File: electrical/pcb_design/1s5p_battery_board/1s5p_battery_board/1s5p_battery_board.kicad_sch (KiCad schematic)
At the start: 0 parts

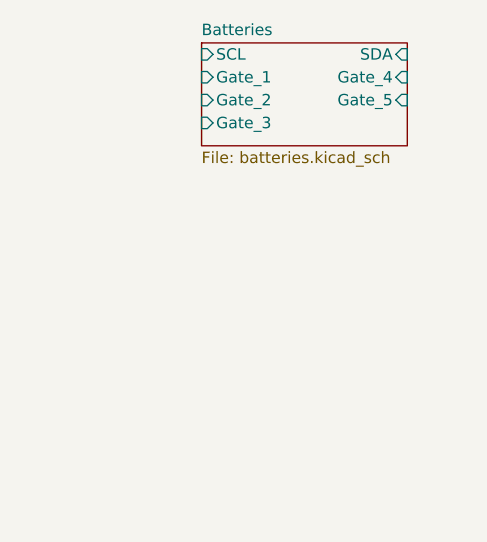
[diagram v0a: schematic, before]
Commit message: mosfet on battery board flipped
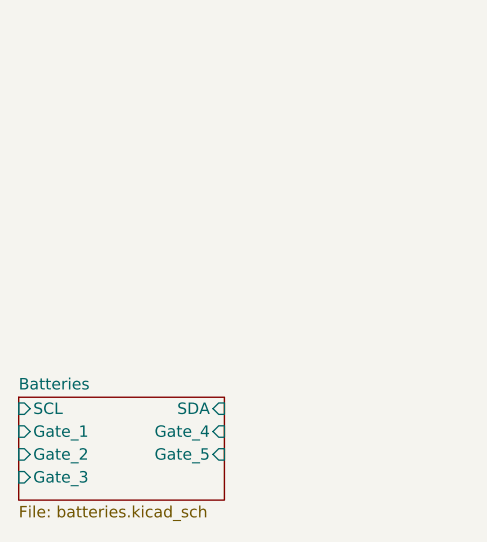
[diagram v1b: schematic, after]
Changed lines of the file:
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@@
 	(paper "A4")
 	(sheet
-		(at 60.96 116.84)
+		(at 40.64 156.21)
 		(size 22.86 11.43)
 		(fields_autoplaced yes)
@@
 		)
 		(property "Sheetname" "Batteries"
-			(at 60.96 116.1284 0)
+			(at 40.64 155.4984 0)
 			(effects
 				(font
@@
 		)
 		(property "Sheetfile" "batteries.kicad_sch"
-			(at 60.96 128.8546 0)
+			(at 40.64 168.2246 0)
 			(effects
 				(font
@@
 		)
 		(pin "Gate_5" input
-			(at 83.82 123.19 0)
+			(at 63.5 162.56 0)
 			(effects
 				(font
@@
 		)
 		(pin "Gate_2" input
-			(at 60.96 123.19 180)
+			(at 40.64 162.56 180)
 			(effects
 				(font
@@
 		)
 		(pin "SCL" input
-			(at 60.96 118.11 180)
+			(at 40.64 157.48 180)
 			(effects
 				(font
@@
 		)
 		(pin "SDA" input
-			(at 83.82 118.11 0)
+			(at 63.5 157.48 0)
 			(effects
 				(font
@@
 		)
 		(pin "Gate_3" input
-			(at 60.96 125.73 180)
+			(at 40.64 165.1 180)
 			(effects
 				(font
@@
 		)
 		(pin "Gate_1" input
-			(at 60.96 120.65 180)
+			(at 40.64 160.02 180)
 			(effects
 				(font
@@
 		)
 		(pin "Gate_4" input
-			(at 83.82 120.65 0)
+			(at 63.5 160.02 0)
 			(effects
 				(font

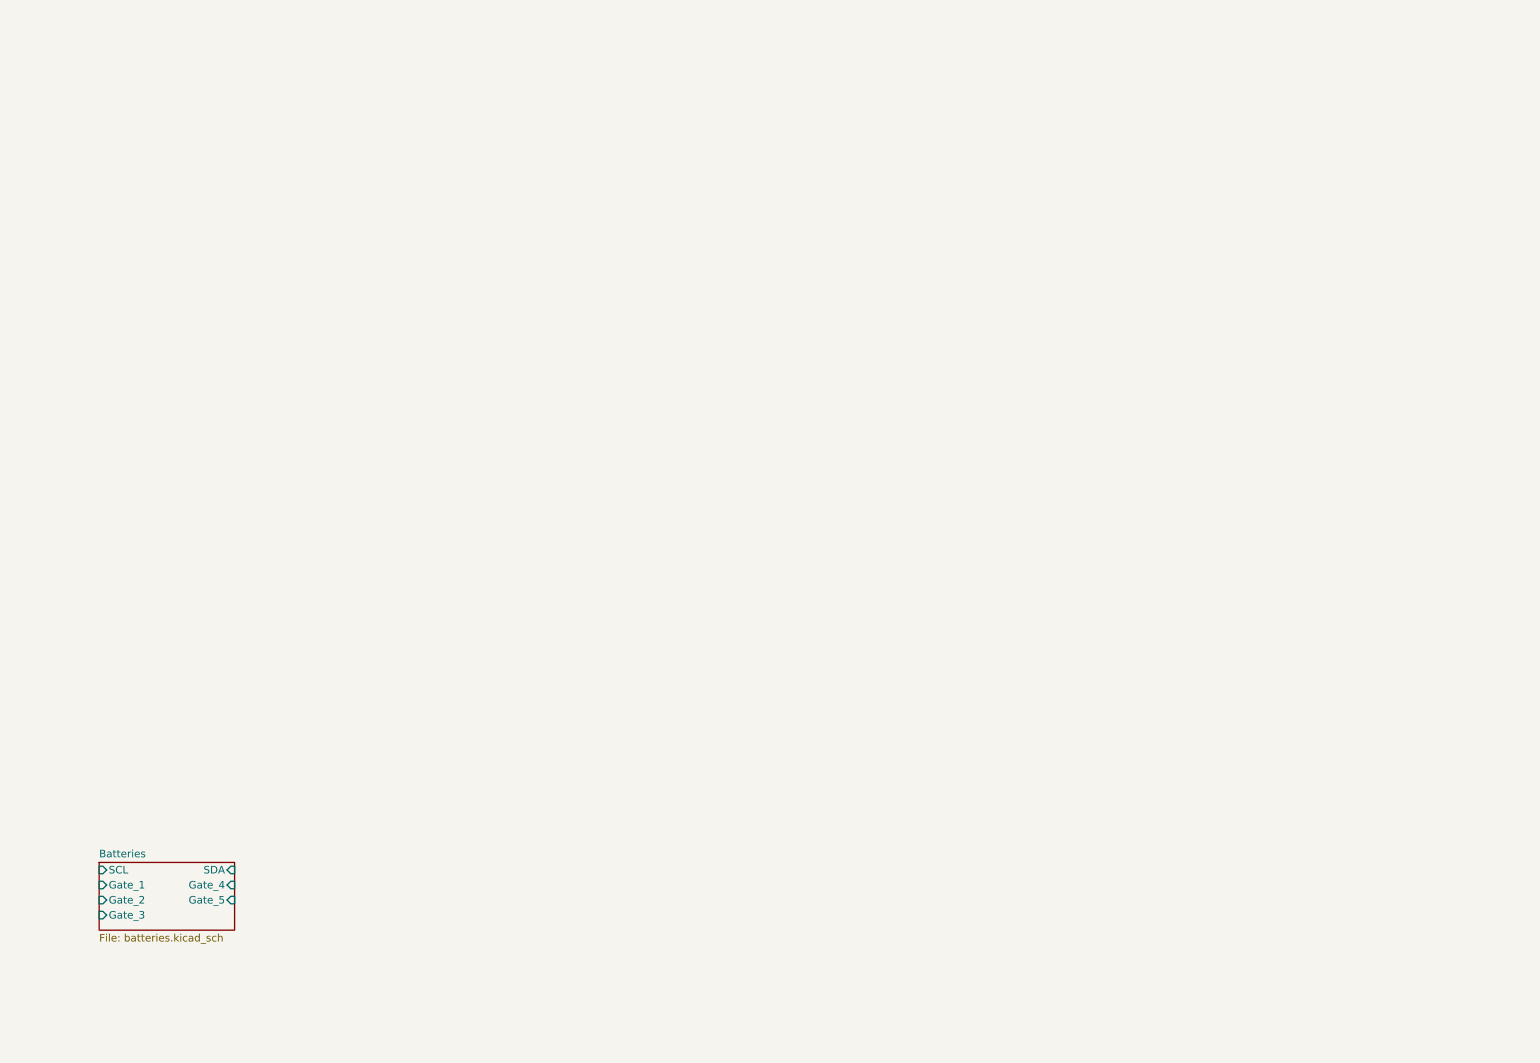
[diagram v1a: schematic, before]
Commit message: added stm32 (with correct stm pinout) and support blocks to battery board
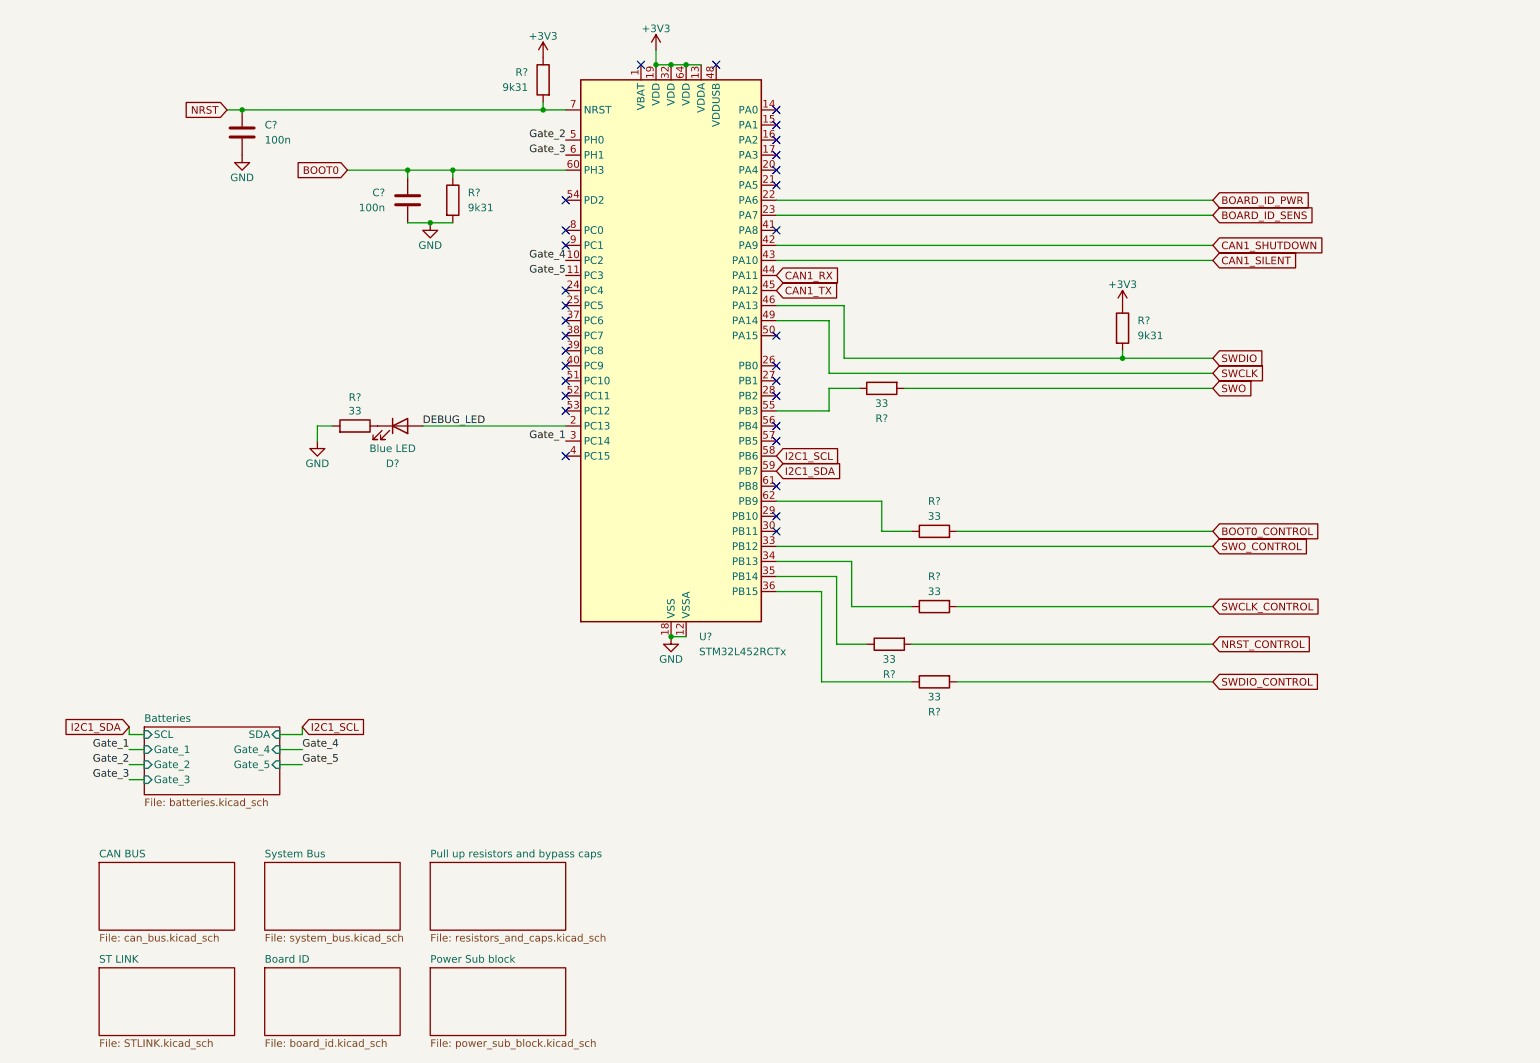
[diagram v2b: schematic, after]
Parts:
- added C? (x2): 100n, footprints:Nondescript_C_0402_1005Metric, symbol Device:C
- added D?: Blue LED, LED_SMD:LED_0603_1608Metric, symbol Device:LED
- added R? (x3): 9k31, footprints:Nondescript_R_0402_1005Metric, symbol Device:R
- added R? (x6): 33, footprints:Nondescript_R_0402_1005Metric, symbol Device:R
- added U?: STM32L452RCTx, Package_QFP:LQFP-64_10x10mm_P0.5mm, symbol MCU_ST_STM32L4:STM32L452RCTx
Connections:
- new net: D?.1 (K), R?.1
- new net: R?.1, U?.36 (PB15)
- new net: R?.1, U?.62 (PB9)
- new net: R?.1, U?.55 (PB3)
- new net: R?.1, U?.34 (PB13)
- new net: R?.1, U?.35 (PB14)
- new net +3V3: R?.1, R?.1, U?.13 (VDDA), U?.19 (VDD), U?.32 (VDD), U?.64 (VDD)
- new net BOARD_ID_PWR: U?.22 (PA6)
- new net BOARD_ID_SENS: U?.23 (PA7)
- new net BOOT0: C?.1, R?.1, U?.60 (PH3)
- new net BOOT0_CONTROL: R?.2
- new net CAN1_RX: U?.44 (PA11)
- new net CAN1_SHUTDOWN: U?.42 (PA9)
- new net CAN1_SILENT: U?.43 (PA10)
- new net CAN1_TX: U?.45 (PA12)
- new net DEBUG_LED: D?.2 (A), U?.2 (PC13)
- new net GND: C?.2, C?.2, R?.2, R?.2, U?.12 (VSSA), U?.18 (VSS), U?.31 (VSS), U?.47 (VSS), U?.63 (VSS)
- new net Gate_1: U?.3 (PC14)
- new net Gate_2: U?.5 (PH0)
- new net Gate_3: U?.6 (PH1)
- new net Gate_4: U?.10 (PC2)
- new net Gate_5: U?.11 (PC3)
- new net I2C1_SCL: U?.58 (PB6)
- new net I2C1_SDA: U?.59 (PB7)
- new net NRST: C?.1, R?.2, U?.7 (NRST)
- new net NRST_CONTROL: R?.2
- new net SWCLK: U?.49 (PA14)
- new net SWCLK_CONTROL: R?.2
- new net SWDIO: R?.2, U?.46 (PA13)
- new net SWDIO_CONTROL: R?.2
- new net SWO: R?.2
- new net SWO_CONTROL: U?.33 (PB12)
- no-connect marks 0 -> 31
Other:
- added sheet Board ID (board_id.kicad_sch)
- added sheet CAN BUS (can_bus.kicad_sch)
- added sheet Power Sub block (power_sub_block.kicad_sch)
- added sheet Pull up resistors and bypass caps (resistors_and_caps.kicad_sch)
- added sheet ST LINK (STLINK.kicad_sch)
- added sheet System Bus (system_bus.kicad_sch)

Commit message: choosing footprints for battery board
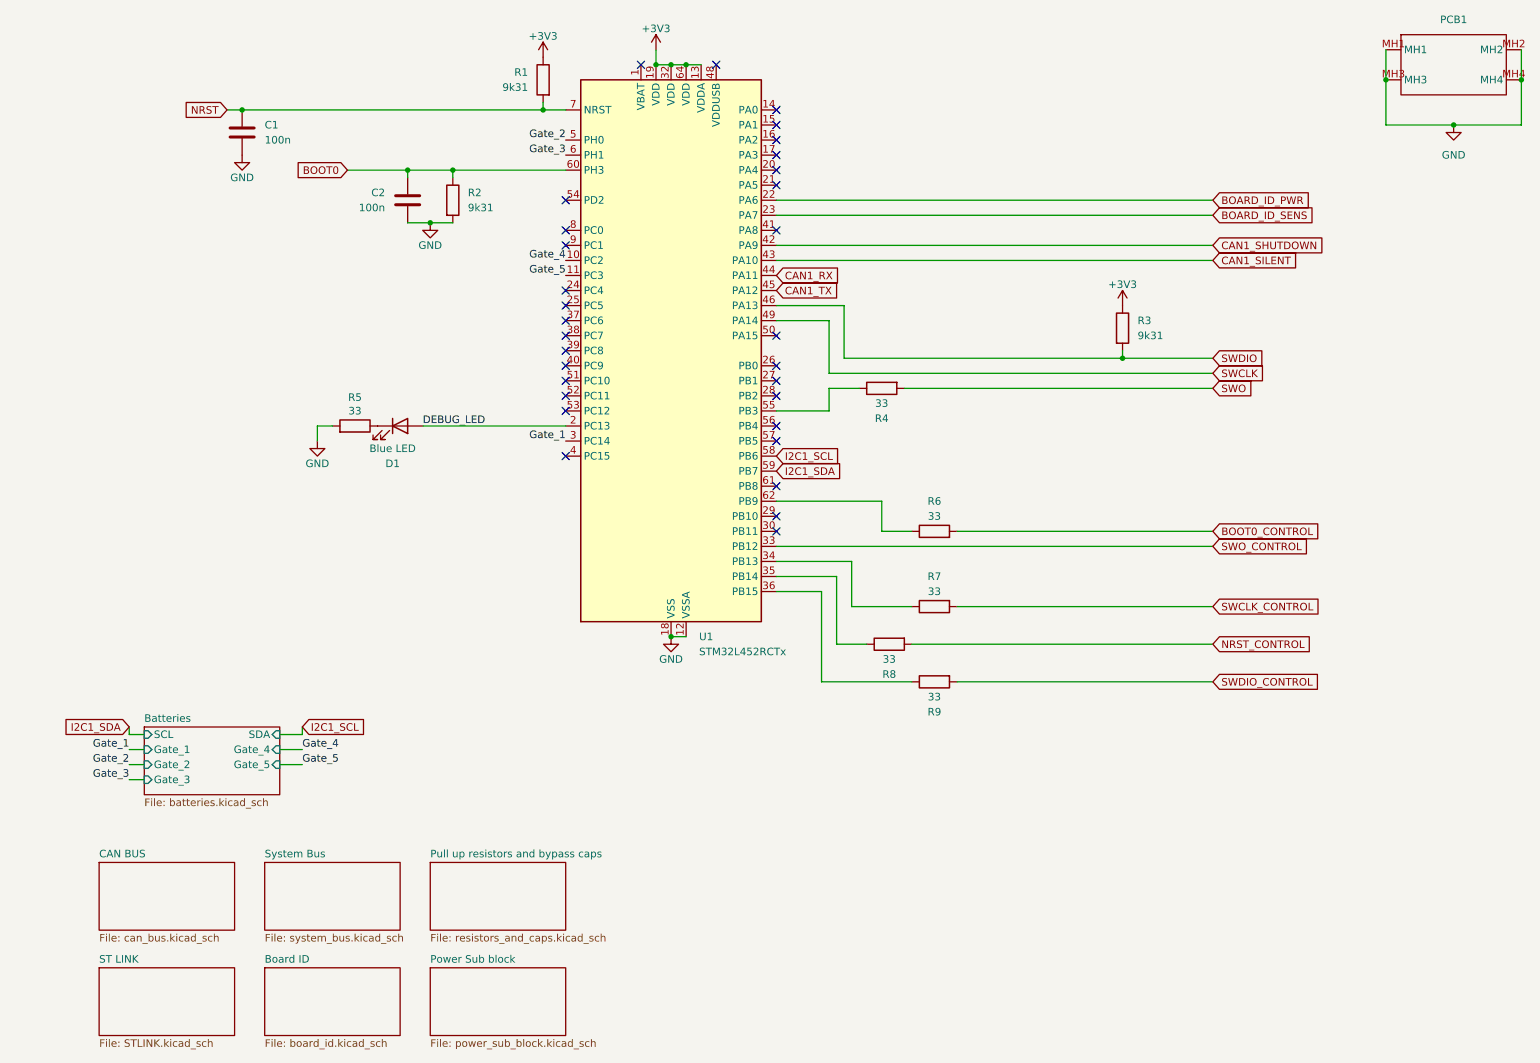
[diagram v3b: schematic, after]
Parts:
- added PCB1: ~, footprints:Core_Board_Shape_Space_Invader_2, symbol tvsc_symbols:Four_Mounting_Hole_PCB
- gave numbers to parts that had none: 13
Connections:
- net GND: now also PCB1.MH1, PCB1.MH2, PCB1.MH3, PCB1.MH4

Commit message: add thermistor, add battery power connector, layout before realizaiton that batteries need to be rotated
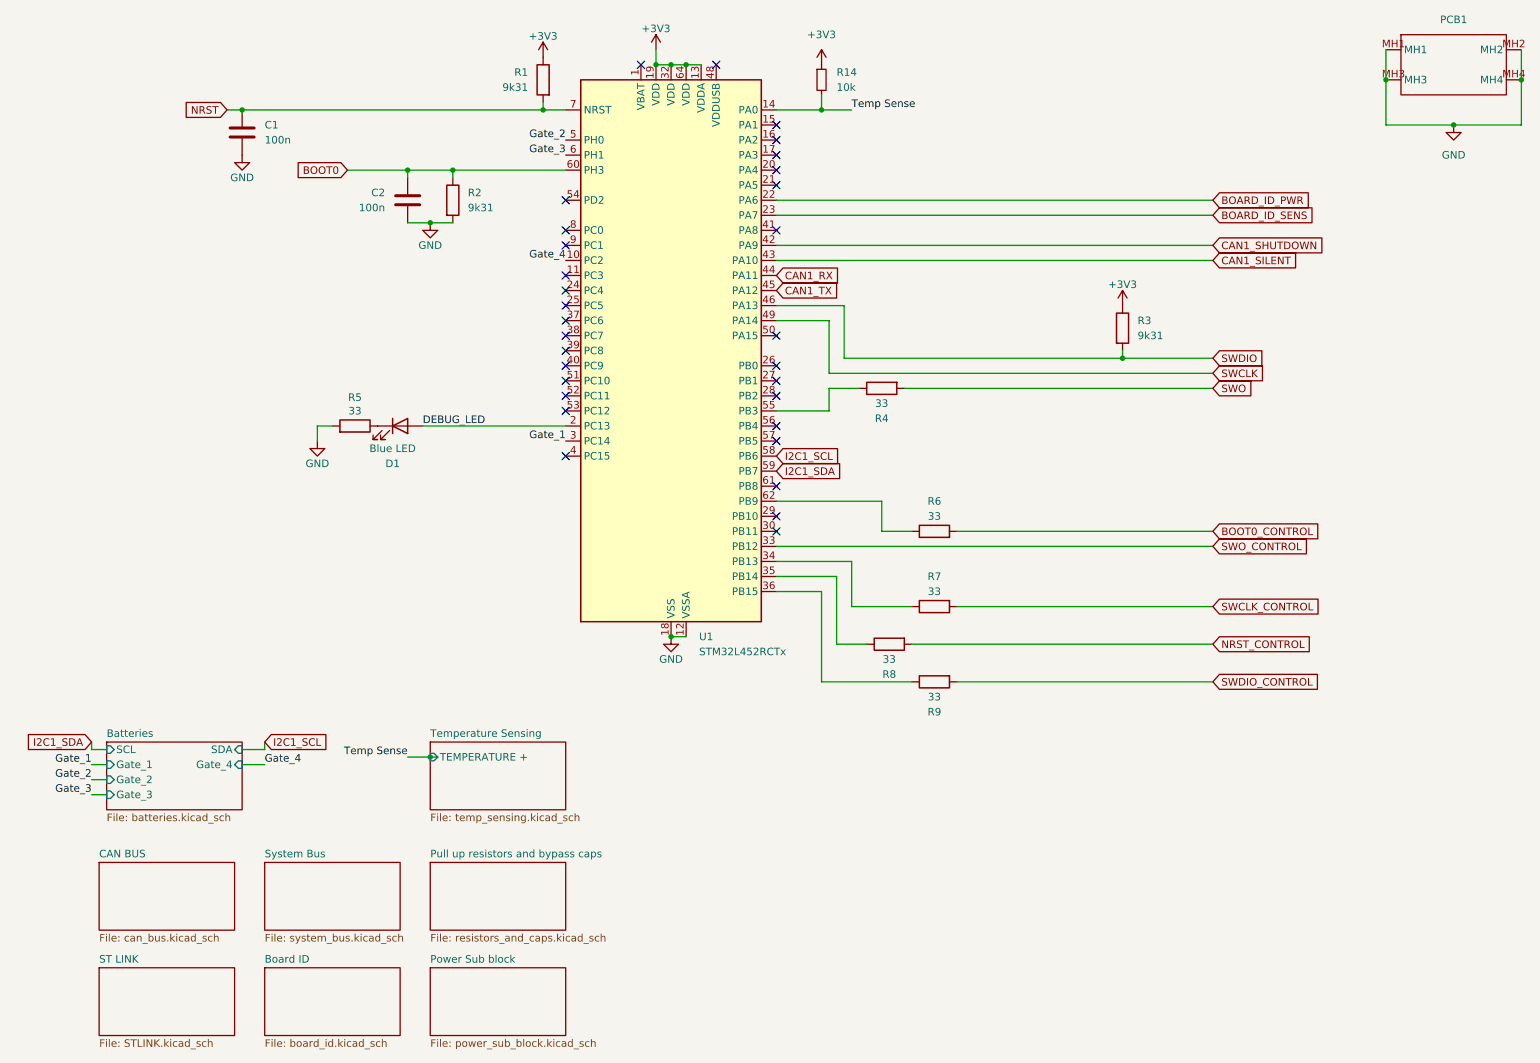
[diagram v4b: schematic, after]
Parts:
- added R14: 10k, footprints:Nondescript_R_0402_1005Metric, symbol Device:R_Small
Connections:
- net +3V3: now also R14.1
- net Temp Sense: now reaches U1.14 (PA0)
- net Temp Sense: now also R14.2
- net Gate_5: no longer names the net of U1.11 (PC3)
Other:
- added sheet Temperature Sensing (temp_sensing.kicad_sch)
- sheet Batteries ports: added none; removed Gate_5
